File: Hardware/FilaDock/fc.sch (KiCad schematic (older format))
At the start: 4 parts, among them J1 Conn_1, J2 Conn_2, J3 PWR_IN, SW1 PowerSel

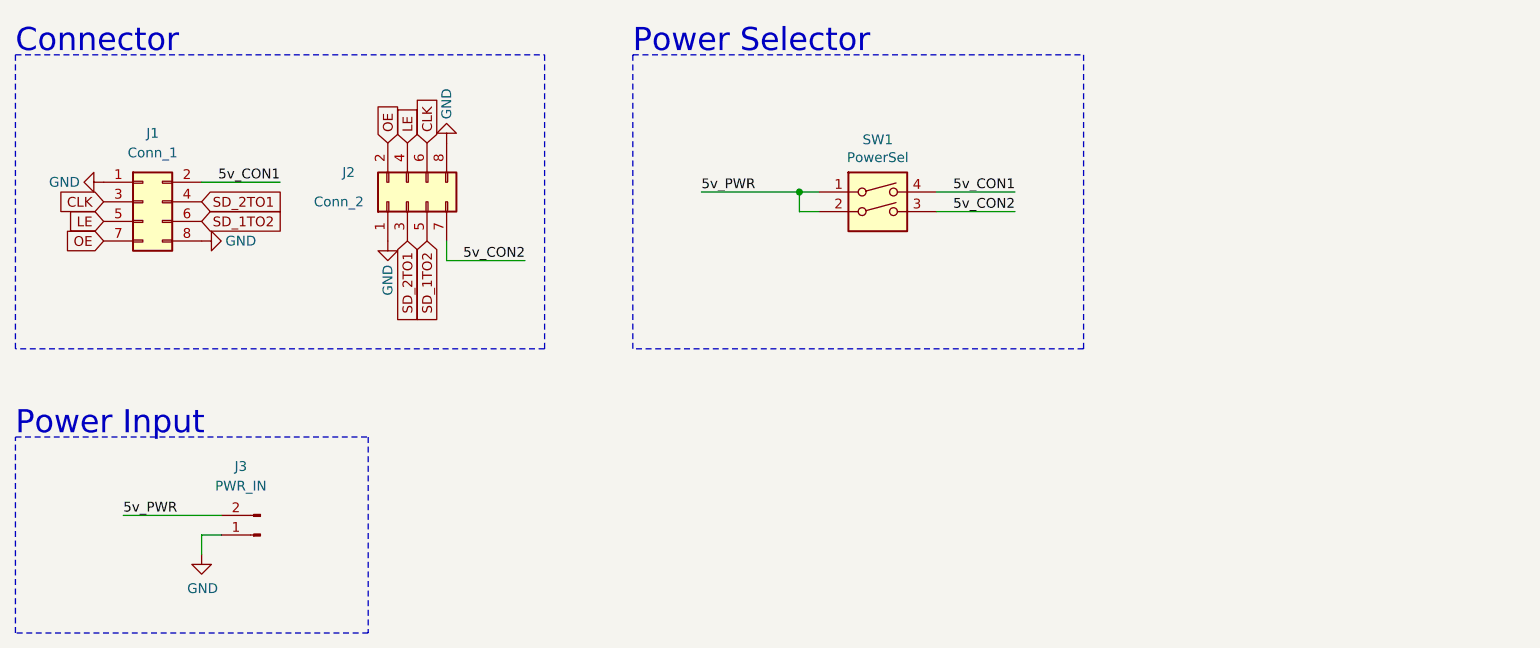
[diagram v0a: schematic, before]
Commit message: Updated FilaDock component
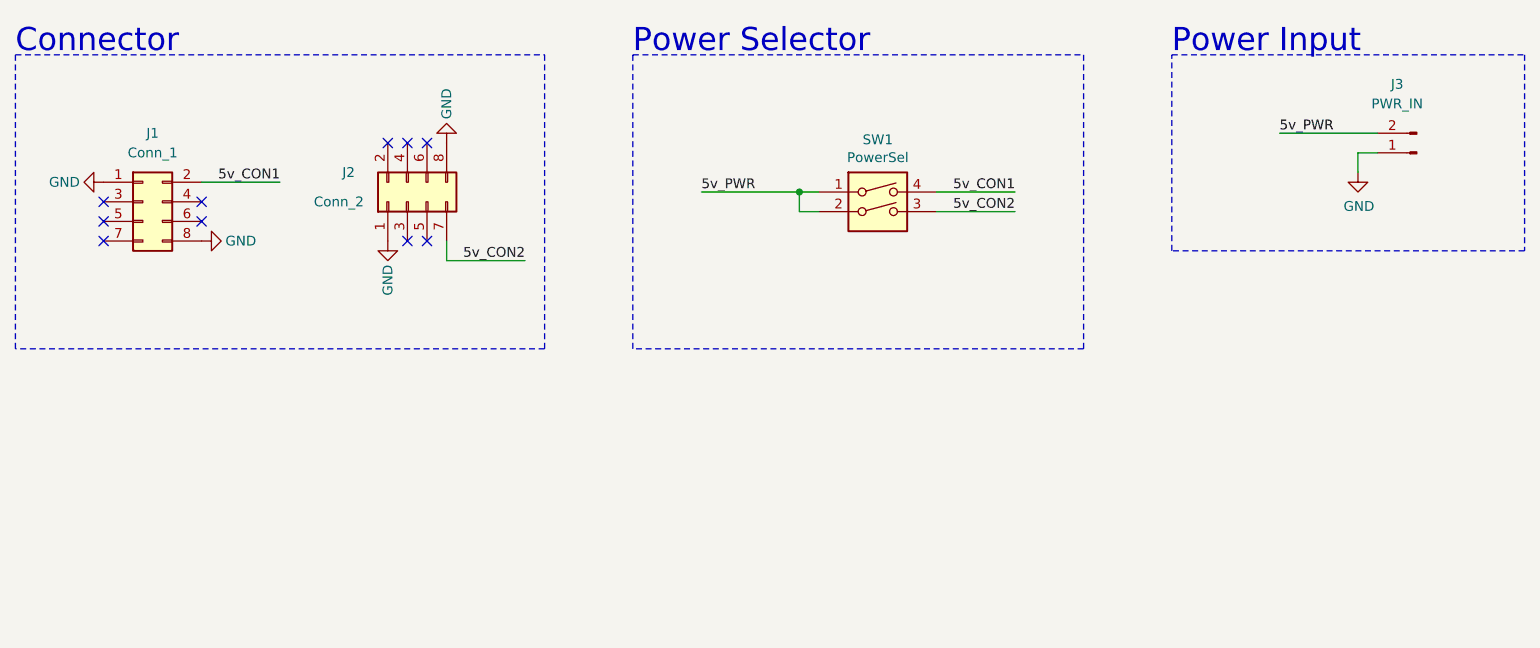
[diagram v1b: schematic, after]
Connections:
- net CLK: no longer names the net of J1.3 (Pin_3)
- net CLK: no longer J2.6 (Pin_6)
- net LE: no longer names the net of J1.5 (Pin_5)
- net LE: no longer J2.4 (Pin_4)
- net OE: no longer names the net of J1.7 (Pin_7)
- net OE: no longer J2.2 (Pin_2)
- net SD_1TO2: no longer names the net of J1.6 (Pin_6)
- net SD_1TO2: no longer J2.5 (Pin_5)
- net SD_2TO1: no longer names the net of J1.4 (Pin_4)
- net SD_2TO1: no longer J2.3 (Pin_3)
- no-connect marks 0 -> 10
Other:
- moved on the sheet: J3
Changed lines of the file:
@@
 	0    -1   -1   0
 $EndComp
-Text GLabel 2950 2500 2    50   Input ~ 0
-SD_1TO2
-Text GLabel 2450 2500 0    50   Input ~ 0
-LE
-Text GLabel 2450 2600 0    50   Input ~ 0
-OE
-Text GLabel 4100 2100 1    50   Input ~ 0
-CLK
-Text GLabel 4000 2100 1    50   Input ~ 0
-LE
-Text GLabel 3900 2100 1    50   Input ~ 0
-OE
-Text GLabel 2450 2400 0    50   Input ~ 0
-CLK
 Text Label 5500 2350 0    50   ~ 0
 5v_PWR
@@
 	1    0    0    -1
 $EndComp
-Text GLabel 2950 2400 2    50   Input ~ 0
-SD_2TO1
 Wire Notes Line
 	2000 1650 4700 1650
@@
 L Connector:Conn_01x02_Male J3
 U 1 1 60677A8B
-P 3250 4100
-F 0 "J3" H 3350 3750 50  0000 C CNN
-F 1 "PWR_IN" H 3350 3850 50  0000 C CNN
-F 2 "Connector_PinHeader_2.54mm:PinHeader_1x02_P2.54mm_Horizontal" H 3250 4100 50  0001 C CNN
-F 3 "~" H 3250 4100 50  0001 C CNN
-	1    3250 4100
+P 9150 2150
+F 0 "J3" H 9250 1800 50  0000 C CNN
+F 1 "PWR_IN" H 9250 1900 50  0000 C CNN
+F 2 "Connector_PinHeader_2.54mm:PinHeader_1x02_P2.54mm_Horizontal" H 9150 2150 50  0001 C CNN
+F 3 "~" H 9150 2150 50  0001 C CNN
+	1    9150 2150
 	-1   0    0    1
 $EndComp
-Text Label 2550 4000 0    50   ~ 0
+Text Label 8450 2050 0    50   ~ 0
 5v_PWR
 Wire Wire Line
-	2550 4000 3050 4000
+	8450 2050 8950 2050
 $Comp
 L power:GND #PWR0106
 U 1 1 60679E8F
-P 2950 4200
-F 0 "#PWR0106" H 2950 3950 50  0001 C CNN
-F 1 "GND" H 2955 4027 50  0000 C CNN
-F 2 "" H 2950 4200 50  0001 C CNN
-F 3 "" H 2950 4200 50  0001 C CNN
-	1    2950 4200
+P 8850 2250
+F 0 "#PWR0106" H 8850 2000 50  0001 C CNN
+F 1 "GND" H 8855 2077 50  0000 C CNN
+F 2 "" H 8850 2250 50  0001 C CNN
+F 3 "" H 8850 2250 50  0001 C CNN
+	1    8850 2250
 	1    0    0    -1
 $EndComp
 Wire Wire Line
-	2950 4200 2950 4100
+	8850 2250 8850 2150
 Wire Wire Line
-	2950 4100 3050 4100
+	8850 2150 8950 2150
 Wire Notes Line
-	2000 3600 3800 3600
+	7900 1650 9700 1650
 Wire Notes Line
-	3800 3600 3800 4600
+	9700 1650 9700 2650
 Wire Notes Line
-	3800 4600 2000 4600
+	9700 2650 7900 2650
 Wire Notes Line
-	2000 4600 2000 3600
-Text Notes 2000 3600 0    118  ~ 0
+	7900 2650 7900 1650
+Text Notes 7900 1650 0    118  ~ 0
 Power Input
 Wire Wire Line
@@
 Wire Notes Line
 	5150 3150 5150 1650
-Text GLabel 4000 2600 3    50   Input ~ 0
-SD_2TO1
 $Comp
 L power:GND #PWR0101
@@
 Text Label 4600 2700 2    50   ~ 0
 5v_CON2
-Text GLabel 4100 2600 3    50   Input ~ 0
-SD_1TO2
+NoConn ~ 4000 2100
+NoConn ~ 3900 2100
+NoConn ~ 4100 2100
+NoConn ~ 4000 2600
+NoConn ~ 4100 2600
+NoConn ~ 2950 2400
+NoConn ~ 2950 2500
+NoConn ~ 2450 2400
+NoConn ~ 2450 2500
+NoConn ~ 2450 2600
 $EndSCHEMATC

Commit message: Update
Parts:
- removed SW1: PowerSel, Button_Switch_SMD:SW_DIP_SPSTx02_Slide_KingTek_DSHP02TS_W7.62mm_P1.27mm, symbol Switch:SW_DIP_x02
- added JP1: SolderJumper_3_Open, Jumper:SolderJumper-3_P1.3mm_Open_RoundedPad1.0x1.5mm, symbol Jumper:SolderJumper_3_Open
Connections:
- net 5v_CON1: now also JP1.1 (A)
- net 5v_CON2: now also JP1.3 (B)
- net 5v_PWR: now also JP1.2 (C)
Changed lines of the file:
@@
 	0    -1   -1   0
 $EndComp
-Text Label 5500 2350 0    50   ~ 0
+Text Label 5750 2350 0    50   ~ 0
 5v_PWR
-Text Label 7100 2350 2    50   ~ 0
+Text Label 6950 2600 2    50   ~ 0
 5v_CON1
-Text Label 7100 2450 2    50   ~ 0
+Text Label 5750 2600 0    50   ~ 0
 5v_CON2
 Text Label 3350 2300 2    50   ~ 0
@@
 	2950 2300 3350 2300
 Wire Wire Line
-	7100 2350 6700 2350
+	6950 2600 6550 2600
 Wire Wire Line
-	6700 2450 7100 2450
+	6150 2600 5750 2600
 $Comp
 L power:GND #PWR0102
@@
 Wire Notes Line
 	2000 3150 2000 1650
-$Comp
-L Switch:SW_DIP_x02 SW1
-U 1 1 606D1845
-P 6400 2450
-F 0 "SW1" H 6400 2817 50  0000 C CNN
-F 1 "PowerSel" H 6400 2726 50  0000 C CNN
-F 2 "Button_Switch_SMD:SW_DIP_SPSTx02_Slide_KingTek_DSHP02TS_W7.62mm_P1.27mm" H 6400 2450 50  0001 C CNN
-F 3 "~" H 6400 2450 50  0001 C CNN
-	1    6400 2450
-	1    0    0    -1
-$EndComp
-Wire Wire Line
-	5500 2350 6000 2350
-Wire Wire Line
-	6100 2450 6000 2450
-Wire Wire Line
-	6000 2450 6000 2350
-Connection ~ 6000 2350
-Wire Wire Line
-	6000 2350 6100 2350
 $Comp
 L Connector:Conn_01x02_Male J3
@@
 NoConn ~ 2450 2500
 NoConn ~ 2450 2600
+$Comp
+L Jumper:SolderJumper_3_Open JP1
+U 1 1 613DBF10
+P 6350 2600
+F 0 "JP1" H 6350 2713 50  0000 C CNN
+F 1 "SolderJumper_3_Open" H 6350 2804 50  0000 C CNN
+F 2 "Jumper:SolderJumper-3_P1.3mm_Open_RoundedPad1.0x1.5mm" H 6350 2600 50  0001 C CNN
+F 3 "~" H 6350 2600 50  0001 C CNN
+	1    6350 2600
+	-1   0    0    1
+$EndComp
+Wire Wire Line
+	5750 2350 6350 2350
+Wire Wire Line
+	6350 2450 6350 2350
 $EndSCHEMATC
